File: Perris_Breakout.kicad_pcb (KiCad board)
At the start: 2 copper layers, 67.3 x 67.3 mm, 21 parts, among them J1 PERRI_1, J10 SDA, J11 GND, J12 GND, J13 SCL, J14 SCL, J2 PERRI_2, J3 PERRI_3, J4 PERRI_4, J5 PERRI_5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

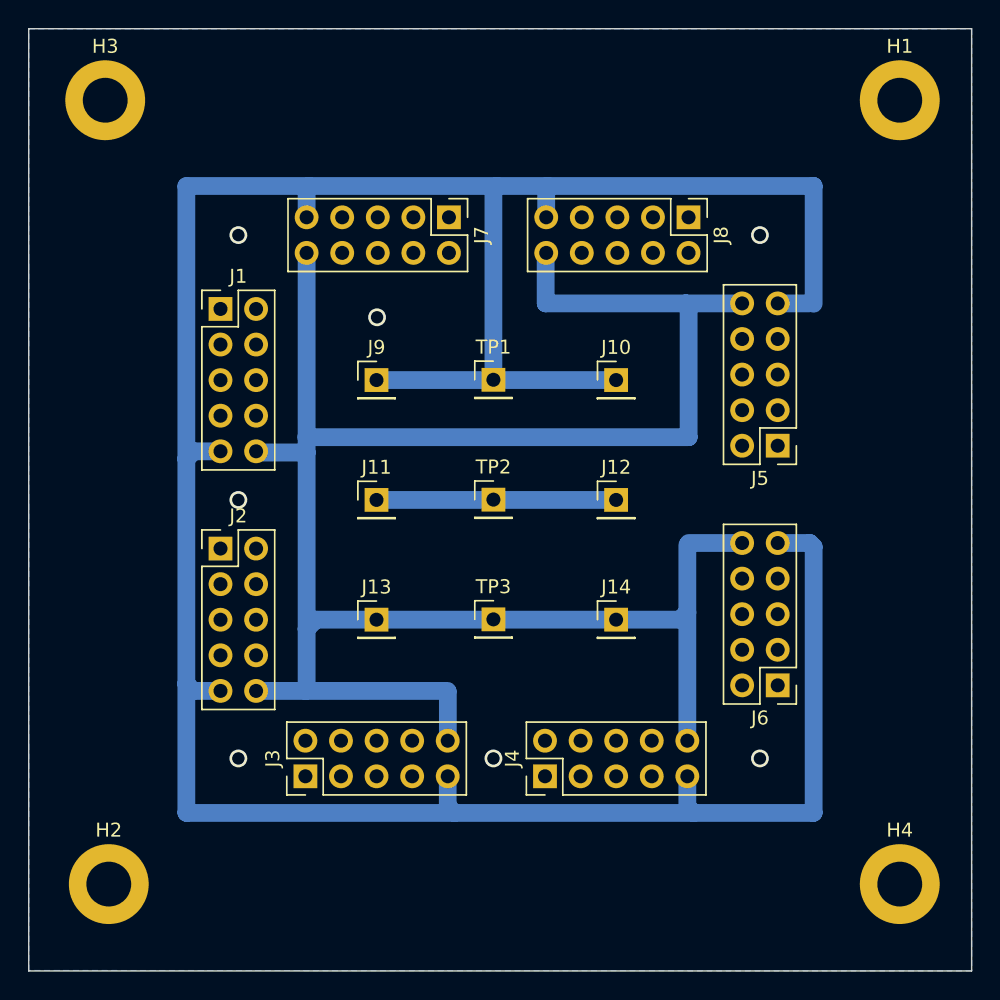
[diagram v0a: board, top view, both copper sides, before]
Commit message: Updated Schematic to add GND, SCL, SDA nets to unused pins. Upated PCB to add filled copper zones for SDA, SCL, and GND nets. Generated new drill and gerber files
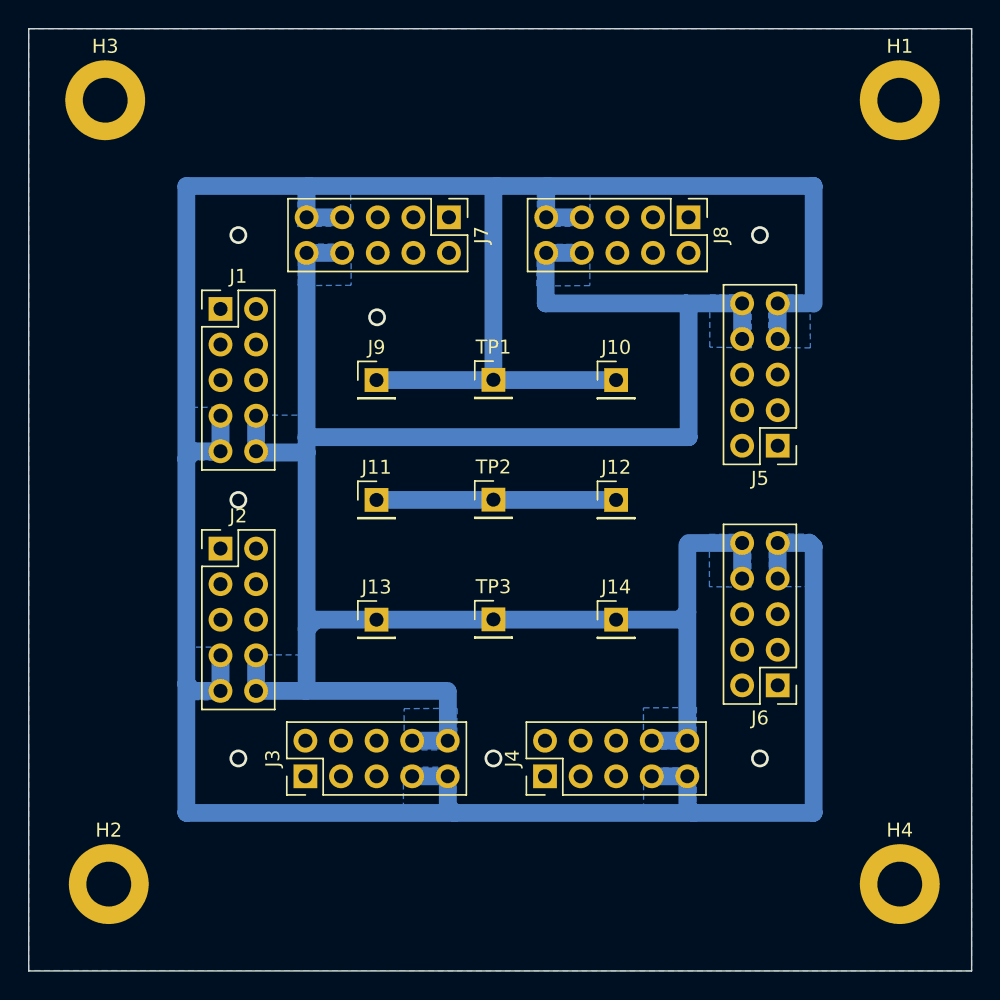
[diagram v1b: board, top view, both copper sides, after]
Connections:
- J1 pad 1: unconnected-(J1-Pad1) -> /GND
- J1 pad 2: unconnected-(J1-Pad2) -> /GND
- J1 pad 4: unconnected-(J1-Pad4) -> /SCL
- J1 pad 7: unconnected-(J1-Pad7) -> /SDA
- J1 pad 9: unconnected-(J1-Pad9) -> /GND
- J2 pad 1: unconnected-(J2-Pad1) -> /GND
- J2 pad 2: unconnected-(J2-Pad2) -> /GND
- J2 pad 4: unconnected-(J2-Pad4) -> /SCL
- J2 pad 7: unconnected-(J2-Pad7) -> /SDA
- J2 pad 9: unconnected-(J2-Pad9) -> /GND
- J3 pad 1: unconnected-(J3-Pad1) -> /GND
- J3 pad 2: unconnected-(J3-Pad2) -> /GND
- J3 pad 4: unconnected-(J3-Pad4) -> /SCL
- J3 pad 7: unconnected-(J3-Pad7) -> /SDA
- J3 pad 9: unconnected-(J3-Pad9) -> /GND
- J4 pad 1: unconnected-(J4-Pad1) -> /GND
- J4 pad 2: unconnected-(J4-Pad2) -> /GND
- J4 pad 4: unconnected-(J4-Pad4) -> /SCL
- J4 pad 7: unconnected-(J4-Pad7) -> /SDA
- J4 pad 9: unconnected-(J4-Pad9) -> /GND
- J5 pad 1: unconnected-(J5-Pad1) -> /GND
- J5 pad 2: unconnected-(J5-Pad2) -> /GND
- J5 pad 4: unconnected-(J5-Pad4) -> /SCL
- J5 pad 7: unconnected-(J5-Pad7) -> /SDA
- J5 pad 9: unconnected-(J5-Pad9) -> /GND
- J6 pad 1: unconnected-(J6-Pad1) -> /GND
- J6 pad 2: unconnected-(J6-Pad2) -> /GND
- J6 pad 4: unconnected-(J6-Pad4) -> /SCL
- J6 pad 7: unconnected-(J6-Pad7) -> /SDA
- J6 pad 9: unconnected-(J6-Pad9) -> /GND
- J7 pad 1: unconnected-(J7-Pad1) -> /GND
- J7 pad 2: unconnected-(J7-Pad2) -> /GND
- J7 pad 4: unconnected-(J7-Pad4) -> /SCL
- J7 pad 7: unconnected-(J7-Pad7) -> /SDA
- J7 pad 9: unconnected-(J7-Pad9) -> /GND
- J8 pad 1: unconnected-(J8-Pad1) -> /GND
- J8 pad 2: unconnected-(J8-Pad2) -> /GND
- J8 pad 4: unconnected-(J8-Pad4) -> /SCL
- J8 pad 7: unconnected-(J8-Pad7) -> /SDA
- J8 pad 9: unconnected-(J8-Pad9) -> /GND
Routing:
- net /SCL: track 152.0 -> 172.4 mm
- net /SDA: track 213.1 -> 233.4 mm
- added copper zone on B.Cu, net /SCL
- added copper zone on B.Cu, net /SDA
